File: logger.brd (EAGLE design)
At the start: 99 x 44.1 mm, 69 parts, among them IC1 LTC4412, J1 POWER_JACKPTH, Q1 FDN360P, Q2 FDN360P, Q3 2N7002PW, Q4 2N7002PW, U1 FT232RL, U2 TPS60150

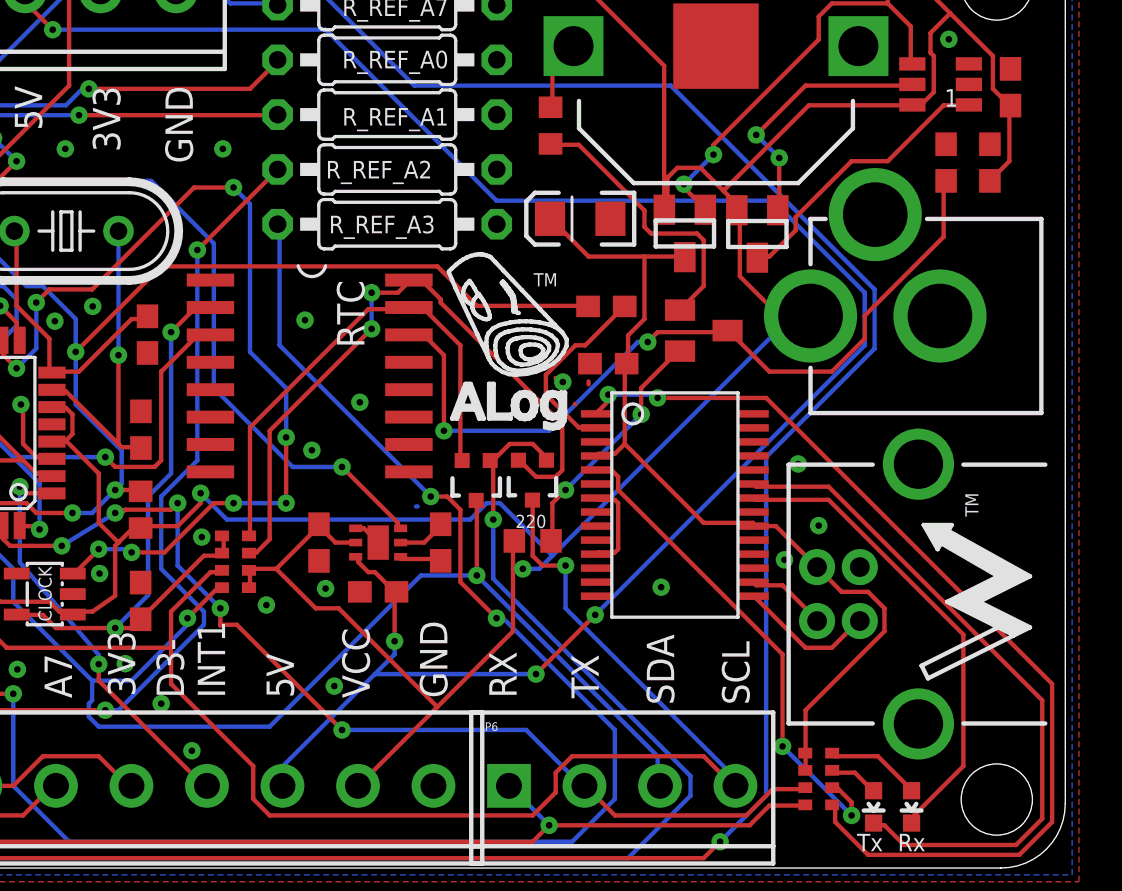
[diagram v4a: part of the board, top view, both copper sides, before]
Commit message: Routed charge pump and gerbers
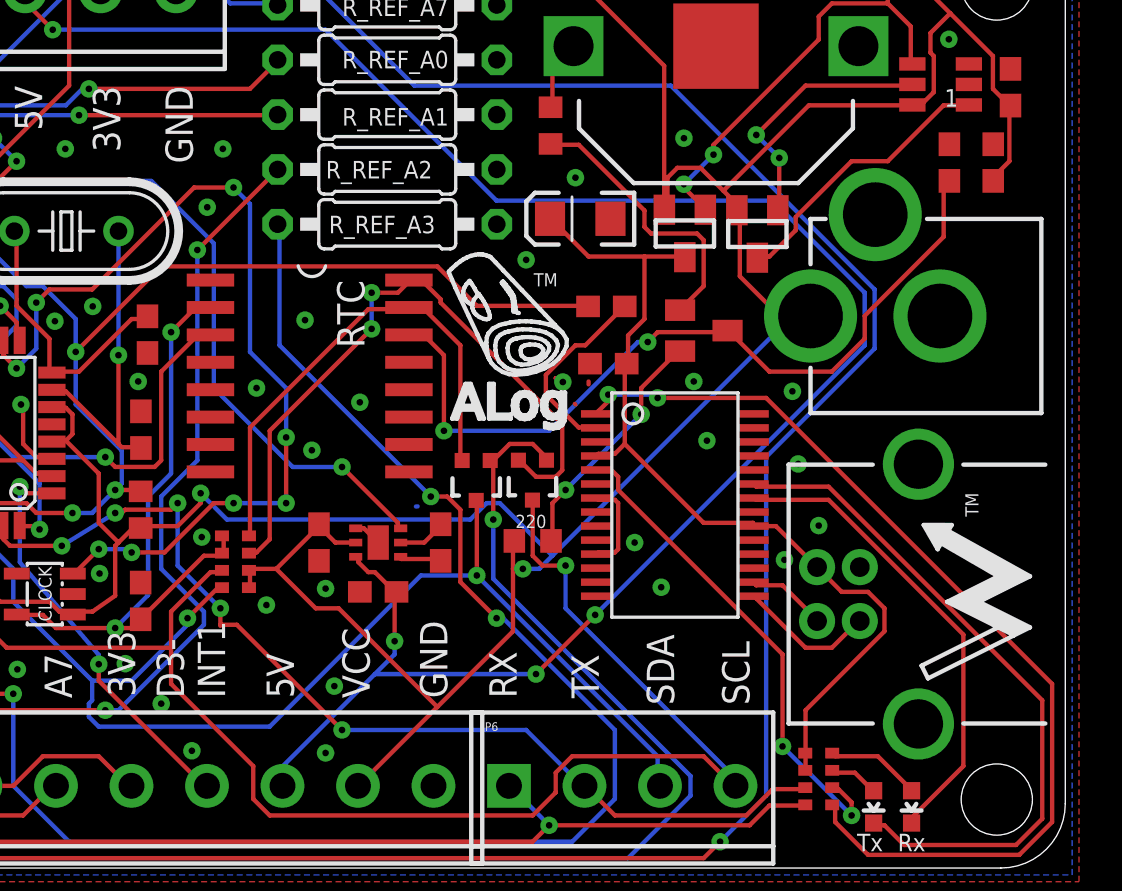
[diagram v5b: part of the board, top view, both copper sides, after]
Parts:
- moved CLOCK_BATT_DECOUP 0.15 mm to (93.7, 32.7)
- moved COUT 0.15 mm to (95.7, 32.7)
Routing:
- net GND: vias 49 -> 60
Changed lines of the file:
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@@
 <?xml version="1.0" encoding="utf-8"?>
 <!DOCTYPE eagle SYSTEM "eagle.dtd">
-<eagle version="6.6.0">
+<eagle version="6.5.0">
 <drawing>
 <settings>
@@
 </element>
 <element name="Q2" library="transistor-power" package="SUPER-SOT3" value="FDN360P" x="81.425" y="29.4175" smashed="yes" rot="R180"/>
-<element name="COUT" library="rcl" package="C0603" value="1uF" x="95.5675" y="32.7025" smashed="yes" rot="R90">
-<attribute name="VALUE" x="97.028" y="33.274" size="0.8128" layer="27" rot="R270"/>
+<element name="COUT" library="rcl" package="C0603" value="1uF" x="95.7199" y="32.7025" smashed="yes" rot="R90">
+<attribute name="VALUE" x="97.028" y="33.5788" size="0.8128" layer="27" rot="R270"/>
 </element>
 <element name="RSTAT" library="rcl" package="R0603" value="470k" x="91.7575" y="41.5925" smashed="yes" rot="R270">
@@
 <element name="LED1" library="SparkFun-LED" package="LED-0603" value="Yellow" x="91.935" y="2.835" smashed="yes" rot="R180"/>
 <element name="LED2" library="SparkFun-LED" package="LED-0603" value="Blue" x="90.1775" y="2.835" smashed="yes" rot="R180"/>
-<element name="CLOCK_BATT_DECOUP" library="rcl" package="C0603" value="1uF" x="93.5355" y="32.7025" smashed="yes" rot="R90"/>
+<element name="CLOCK_BATT_DECOUP" library="rcl" package="C0603" value="1uF" x="93.6879" y="32.7025" smashed="yes" rot="R90"/>
 <element name="D1" library="semicon-smd-ipc" package="SOT23C" value="BAT54C" x="82.305" y="24.9125" smashed="yes" rot="R270">
 <attribute name="VALUE" x="79.63" y="26.6175" size="0.6096" layer="27" rot="R270"/>
@@
 <wire x1="96.4692" y1="32.766" x2="95.7072" y2="32.004" width="0.2032" layer="1"/>
 <wire x1="96.4692" y1="35.2044" x2="96.4692" y2="32.766" width="0.2032" layer="1"/>
-<wire x1="95.7072" y1="32.004" x2="95.5675" y2="31.8525" width="0.2032" layer="1"/>
+<wire x1="95.7072" y1="32.004" x2="95.7199" y2="31.8525" width="0.2032" layer="1"/>
 <wire x1="96.4692" y1="35.2044" x2="96.52" y2="35.345" width="0.2032" layer="1"/>
 <wire x1="92.6592" y1="40.6908" x2="91.8972" y2="40.6908" width="0.2032" layer="1"/>
@@
 <wire x1="85.344" y1="23.0124" x2="88.2396" y2="23.0124" width="0.2032" layer="1"/>
 <wire x1="83.5152" y1="24.8412" x2="85.344" y2="23.0124" width="0.2032" layer="1"/>
-<wire x1="93.4212" y1="31.8516" x2="93.5355" y2="31.8525" width="0.2032" layer="1"/>
+<wire x1="93.4212" y1="31.8516" x2="93.6879" y2="31.8525" width="0.2032" layer="1"/>
 <wire x1="83.5152" y1="24.8412" x2="83.405" y2="24.9125" width="0.2032" layer="1"/>
 <wire x1="69.342" y1="24.6888" x2="68.7324" y2="24.6888" width="0.2032" layer="1"/>
@@
 <wire x1="42.672" y1="19.6596" x2="43.3895" y2="19.6596" width="0.2032" layer="1"/>
 <wire x1="43.3895" y1="19.6596" x2="43.4975" y2="19.7676" width="0.2032" layer="1"/>
-<wire x1="66.167" y1="15.748" x2="64.4652" y2="14.2376" width="0" layer="19" extent="1-1"/>
-<wire x1="56.2102" y1="21.17" x2="59.4334" y2="20.9042" width="0" layer="19" extent="1-1"/>
-<wire x1="53.975" y1="26.035" x2="56.515" y2="23.8769" width="0" layer="19" extent="1-1"/>
+<via x="61.5696" y="22.2504" extent="1-16" drill="0.3048" shape="octagon"/>
+<via x="56.0832" y="22.5552" extent="1-16" drill="0.3048" shape="octagon"/>
+<via x="64.77" y="5.334" extent="1-16" drill="0.3048" shape="octagon"/>
+<via x="81.3816" y="33.8328" extent="1-16" drill="0.3048" shape="octagon"/>
+<via x="76.3524" y="32.004" extent="1-16" drill="0.3048" shape="octagon"/>
+<via x="59.2836" y="30.6324" extent="1-16" drill="0.3048" shape="octagon"/>
+<via x="74.0664" y="28.194" extent="1-16" drill="0.3048" shape="octagon"/>
+<via x="79.0956" y="15.0876" extent="1-16" drill="0.3048" shape="octagon"/>
+<via x="82.4484" y="19.812" extent="1-16" drill="0.3048" shape="octagon"/>
+<via x="81.8388" y="22.5552" extent="1-16" drill="0.3048" shape="octagon"/>
+<via x="86.4108" y="22.098" extent="1-16" drill="0.3048" shape="octagon"/>
 </signal>
 <signal name="5V">

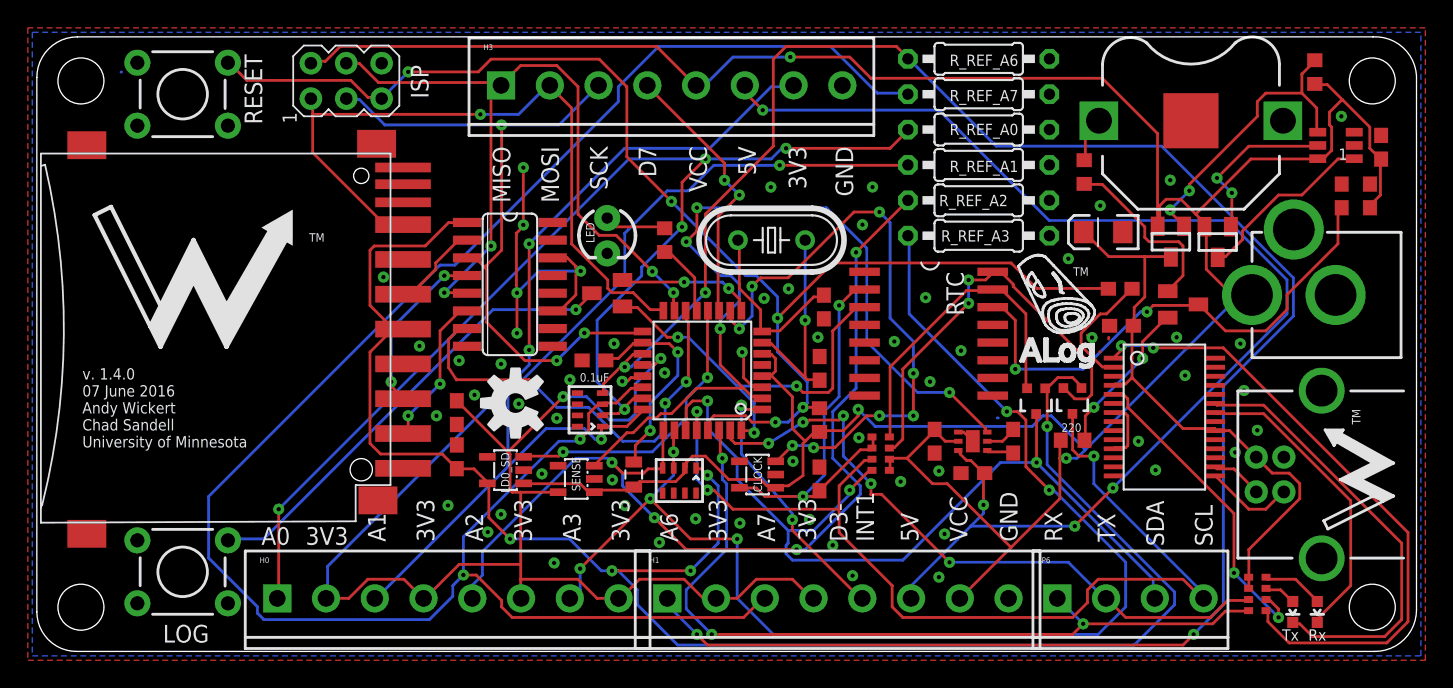
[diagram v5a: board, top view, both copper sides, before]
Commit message: Updated BOM and board layout with cheaper and smaller component packages
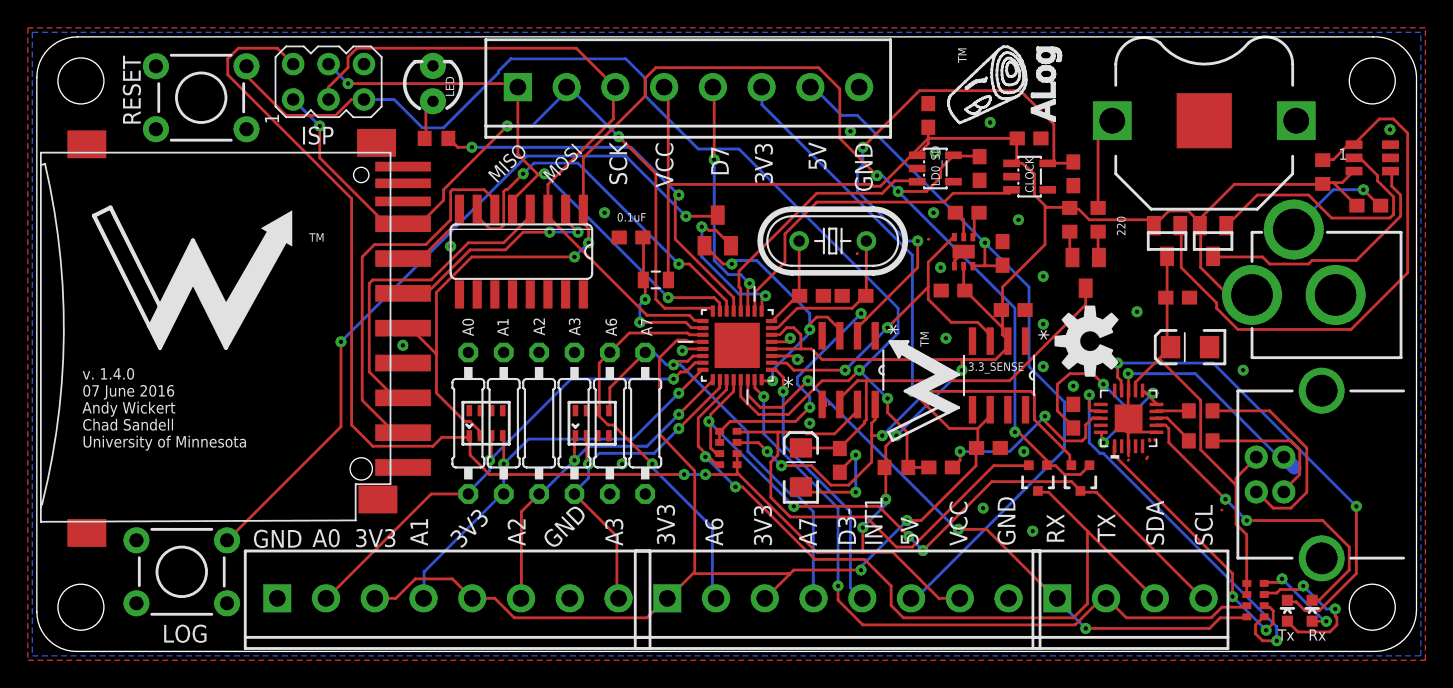
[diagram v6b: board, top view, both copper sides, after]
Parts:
- removed C_LDO_SENSE1, DECOUP: 2.2uF, resistor:C0603
- removed RTC: DS3231SN, comfile:SO16W
- removed R_REF_A0, R_REF_A1, R_REF_A2, R_REF_A3, R_REF_A6, R_REF_A7: (no value), resistor:0207/10
- removed SENSE: LP2985, adafruit:SOT23-5L
- added 3.3_SENSE: LT1461DHS8-5PBF, LTC_By_element14_Batch_1:SOIC127P600X175-8N
- added 5V_CHARGE_PUMP: TPS60150, ti_by_element14:SON65P200X200X80-7N
- added A0, A1, A2, A3, A6, A7: (no value), resistor:0207/10
- added C1: 0.1uF, resistor:C0603
- added CLOCK_BATT_DECOUPLE: 10uF, SparkFun-Passives:EIA3216
- added CLOCK_CIN, SD_CIN, SENSE_CIN: 1uF, rcl:C0603
- added C_LDO_CLOCK: 2.2uF, resistor:C0603
- added D+, D-: 27ohm, rcl:R0603
- CLOCK_BATT_DECOUP: value 1uF -> 0.1uF
- MCU: value ATMega328 -> ATMEGA328P-MU; device SparkFun:TQFP32-08 -> Atmel_By_element14_Batch_1-00:QFN50P500X500X100-33N
- U1: value FT232RL -> DS3231MZ/V+T; device SparkFun-DigitalIC:SSOP28DB -> Maxim-DS3231MZ_8-SOIC:21-0041B_8
- U2: value TPS60150 -> FT231X-Q; device ti_by_element14:SON65P200X200X80-7N -> FT231X:QFN20
- moved C_LDO_SD 42.9 mm to (67.7, 34.7), turned to 90 degrees
- moved LOGO1 41.5 mm to (75.6, 22.3)
- moved CLOCK_BATT_DECOUP 40.7 mm to (57.7, 13.7), turned to 270 degrees
- moved C_LDO_SENSE 38.2 mm to (68.3, 14.6), turned to 180 degrees
- moved LD0_SD 37.7 mm to (64.5, 34.7), turned to 270 degrees
- moved U$3 31.9 mm to (63.2, 18.7)
- moved CLOCK 29.0 mm to (71.3, 34.1), turned to 270 degrees
- moved U1 22.9 mm to (58.3, 20.2)
- moved COUT1 18.2 mm to (64.9, 13.2)
- moved R_LED 17.9 mm to (28.7, 36.8), turned to 180 degrees
- moved C_BOOST_2 16.7 mm to (66.8, 31.5), turned to 0 degrees
- moved LED 16.6 mm to (28.4, 40.8), turned to 90 degrees
- moved U$2 16.0 mm to (68.3, 40.8), turned to 90 degrees
- moved C_BOOST_3 15.9 mm to (69.3, 28.6), turned to 270 degrees
- moved RCKL1 15.8 mm to (74.2, 31.0), turned to 90 degrees
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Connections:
- new net N$13: D-.1, U2.9
- new net N$16: D+.1, U2.8
- new net N$17: C1.1, U2.10, U2.11, U2.20
- net +3V3: now also 3.3_SENSE.6, H0.3, H0.5, H1.1, H1.3, H3.6; no longer H0.2, H0.4, H0.6, H0.8, H1.2, H1.4, H3.7, SENSE.5
- net 5V: now also 5V_CHARGE_PUMP.3, H3.7; no longer H3.6, U2.3
- net A0: now also A0.2, C14.C1, H0.2; no longer C15.B1, H0.1, R_REF_A0.2
- net A1: now also A1.2, C14.D1, H0.4; no longer C15.A1, H0.3, R_REF_A1.2
- net A2: now also A2.2, C15.A1, H0.6; no longer C14.D1, H0.5, R_REF_A2.2
- net A3: now also A3.2, C15.B1, H0.8; no longer C14.C1, H0.7, R_REF_A3.2
- net A6: now also A6.1, C15.C2, H1.2; no longer C15.D1, H1.1, R_REF_A6.2
- net A7: now also A7.1, C15.D2, H1.4; no longer C15.C1, H1.3, R_REF_A7.2
- net BAT: now also CLOCK_BATT_DECOUPLE.A, U1.6; no longer RTC.14
- net D4-SENSE_LDO_SWITCH: now also 3.3_SENSE.3, 5V_CHARGE_PUMP.6; no longer SENSE.3, U2.6
- net D7-CS-EXT: now also H3.5; no longer H3.4
- net DTR: now also U2.18; no longer U1.2
- net GND: now also 3.3_SENSE.4, 5V_CHARGE_PUMP.1, 5V_CHARGE_PUMP.7, A0.1, A1.1, A2.1, A3.1, A6.2, A7.2, C1.2, C15.C1, C15.D1, CLOCK_BATT_DECOUPLE.C, CLOCK_CIN.2, C_LDO_CLOCK.1, H0.1, H0.7, SD_CIN.2, SENSE_CIN.2, U1.5, U2.13, U2.21, U2.3, U2.6; no longer C15.C2, C15.D2, C_LDO_SENSE1.1, DECOUP.2, RTC.10, RTC.11, RTC.12, RTC.13, RTC.5, RTC.6, RTC.7, RTC.8, RTC.9, R_REF_A0.1, R_REF_A1.1, R_REF_A2.1, R_REF_A3.1, R_REF_A6.1, R_REF_A7.1, SENSE.2, U1.11, U1.18, U1.21, U1.25, U1.26, U1.7, U2.1, U2.7
- net INT0: now also U1.3; no longer RTC.3
- net N$14: now also 5V_CHARGE_PUMP.4; no longer U2.4
- net N$15: now also 5V_CHARGE_PUMP.5; no longer U2.5
- net N$27: now also U2.17; no longer U1.1
- net N$29: now also U2.1; no longer U1.5
- net N$3: now also D+.2; no longer U1.15
- net N$4: now also D-.2; no longer U1.16
- net N$5: now also U2.7; no longer U1.22
- net N$6: now also U2.14; no longer U1.23
- net SCL_3V3: now also U1.8; no longer RTC.16
- net SDA_3V3: now also U1.7; no longer RTC.15
- net VCC: now also 3.3_SENSE.2, 5V_CHARGE_PUMP.2, C14.A1, CLOCK_CIN.1, H3.4, SD_CIN.1, SENSE_CIN.1; no longer C14.B1, DECOUP.1, H3.5, SENSE.1, U2.2
- net VCL: now also C_LDO_CLOCK.2, U1.2; no longer C_LDO_SENSE1.2, RTC.2
- net VDD: now also C14.B1; no longer C14.A1
- net VUSB: now also U2.12; no longer U1.20, U1.4
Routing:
- net A6: track 144.4 -> 29.1 mm, vias 4 -> 1
- net A7: track 136.7 -> 31.5 mm, vias 2 -> 1
- net A3: track 91.7 -> 25.8 mm, vias 6 -> 2
- net A0: track 88.6 -> 36.4 mm, vias 5 -> 2
- net A2: track 69.5 -> 25.7 mm, vias 4 -> 2
- net D4-SENSE_LDO_SWITCH: track 62.8 -> 25.2 mm, vias 4 -> 2
- net A1: track 68.6 -> 31.3 mm
- net 5V: track 90.3 -> 53.6 mm, vias 4 -> 1
- net VDD: track 128.8 -> 100.6 mm
- net VCL: track 29.2 -> 56.8 mm, vias 2 -> 4
- net +3V3: track 132.3 -> 109.0 mm, vias 4 -> 3
- net D9_LED: track 5.38 -> 28.4 mm, vias 0 -> 2
- net SCL: track 73.5 -> 51.5 mm, vias 3 -> 4
- net GND: track 36.2 -> 55.7 mm, vias 60 -> 29
- net N$7: track 21.4 -> 40.8 mm, vias 2 -> 0
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
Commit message: 33pF decoupling on USB data; Rx Tx LED flip
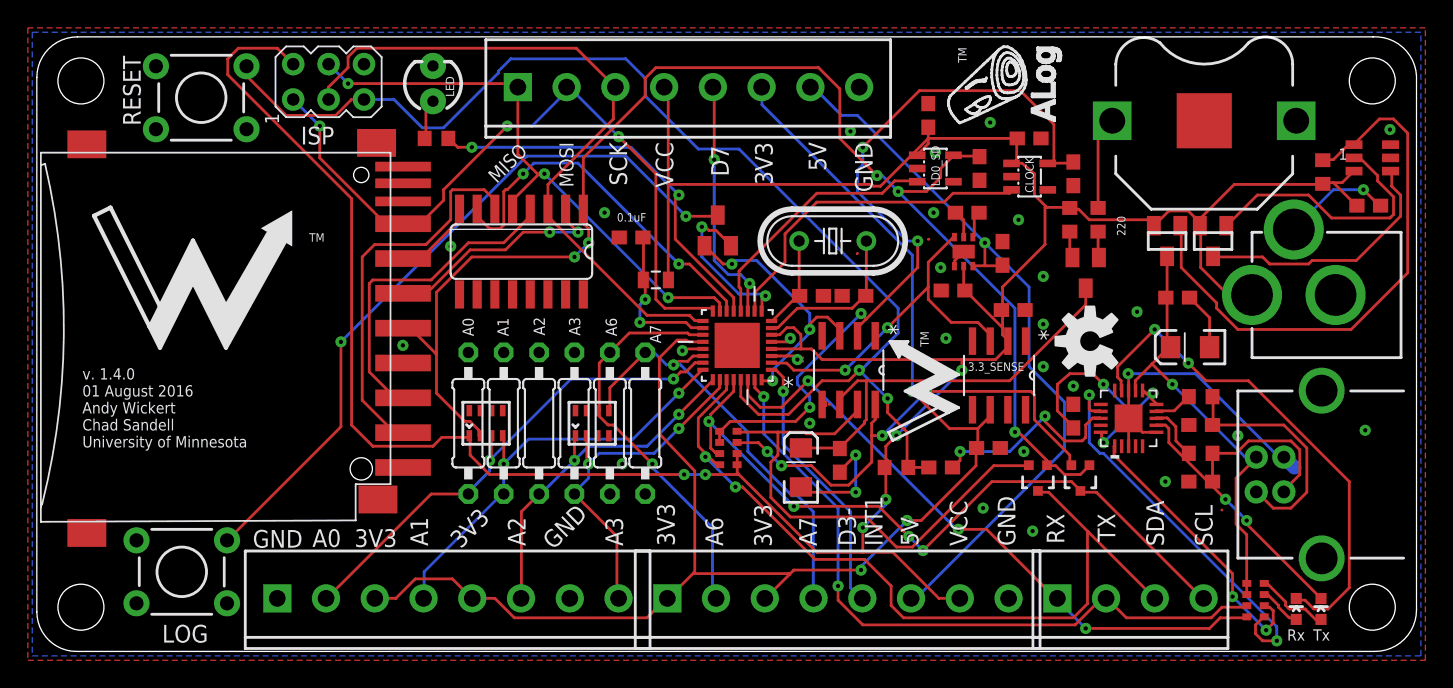
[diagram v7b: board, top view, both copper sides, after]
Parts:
- added CX2, CX3: 33pF, resistor:C0603
- moved LED2 2.42 mm to (92.2, 3.05)
- moved LED1 1.15 mm to (90.4, 3.05)
- moved D- 1.02 mm to (83.6, 18.3)
- moved D+ 0.89 mm to (83.6, 14.2)
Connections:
- net GND: now also CX2.1, CX3.1
- net N$10: now also LED1.C, U2.14; no longer LED2.A, RN1.3
- net N$3: now also CX3.2
- net N$4: now also CX2.2
- net N$5: now also LED2.A, RN1.4; no longer LED1.C, U2.7
- net N$6: now also U2.7; no longer U2.14
- net N$9: now also RN1.3; no longer RN1.4
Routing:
- net N$10: track 11.4 -> 36.5 mm
- net N$5: track 23.3 -> 5.32 mm, vias 2 -> 0
- net N$6: track 34.8 -> 17.7 mm
- net N$9: track 6.91 -> 3.18 mm, vias 2 -> 0
- net N$3: track 10.0 -> 12.4 mm
- net GND: track 55.7 -> 57.6 mm, vias 29 -> 31
- net N$4: track 15.6 -> 17.3 mm
- net VUSB: track 33.3 -> 32.0 mm, vias 0 -> 1
- net N$16: track 3.22 -> 4.00 mm
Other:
- board text added: "v. 1.4.0 01 August 2016 Andy Wickert Chad Sandell University of Minnesota"
- board text removed: "v. 1.4.0 07 June 2016 Andy Wickert Chad Sandell University of Minnesota"
